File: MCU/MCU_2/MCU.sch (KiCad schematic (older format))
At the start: 41 parts, among them J10 RotEnc, J2 Conn_01x08, J3 Conn_02x20_Odd_Even, J4 SWD, U1 74HC04, U2 STM32F407VETx, Y1 12MHz

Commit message: MCU PCB start layouting
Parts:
- J2: value Conn_01x08 -> LPF
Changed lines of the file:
@@
 P 1800 5350
 F 0 "J2" V 1764 5730 50  0000 L CNN
-F 1 "Conn_01x08" V 1673 5730 50  0000 L CNN
+F 1 "LPF" V 1673 5730 50  0000 L CNN
 F 2 "Connector_JST:JST_PH_B8B-PH-SM4-TB_1x08-1MP_P2.00mm_Vertical" H 1800 5350 50  0001 C CNN
 F 3 "~" H 1800 5350 50  0001 C CNN
@@
 	6050 7250 6050 7400
 $Comp
-L power:GND #PWR?
+L power:GND #PWR0121
 U 1 1 62014679
 P 6150 7300
-F 0 "#PWR?" H 6150 7050 50  0001 C CNN
+F 0 "#PWR0121" H 6150 7050 50  0001 C CNN
 F 1 "GND" V 6155 7172 50  0000 R CNN
 F 2 "" H 6150 7300 50  0001 C CNN
@@
 	6150 7350 6150 7400
 $Comp
-L power:GND #PWR?
+L power:GND #PWR0131
 U 1 1 62098915
 P 5700 7400
-F 0 "#PWR?" H 5700 7150 50  0001 C CNN
+F 0 "#PWR0131" H 5700 7150 50  0001 C CNN
 F 1 "GND" V 5705 7272 50  0000 R CNN
 F 2 "" H 5700 7400 50  0001 C CNN

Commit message: routing signals
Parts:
- removed C5: 104, lc_lib:0805_C, symbol Device:C_Small
- removed L2, L3, L6, L7: 600Ohm, lc_lib:0805_L, symbol Device:Ferrite_Bead_Small
- added C37, C40: 104, lc_lib:0805_C, symbol Device:C_Small
- C1, C2: value C_Small -> 20
- J4: footprint Connector_JST:JST_PH_B4B-PH-SM4-TB_1x04-1MP_P2.00mm_Vertical -> Connector_PinHeader_2.54mm:PinHeader_1x04_P2.54mm_Vertical
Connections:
- net +3V3: now also C37.2, C40.1
- net GNDD: now also C37.1, C40.2
- net RX: now also U2.69 (PA10)
- net RX3: now also U2.48 (PB11)
- net TX: now also U2.68 (PA9)
- net TX3: now also U2.47 (PB10)
- net \PTT_SUPPRESS: now also U2.87 (PD6); no longer U2.65 (PC8)
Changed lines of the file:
@@
 P 3200 3100
 F 0 "C2" V 2971 3100 50  0000 C CNN
-F 1 "C_Small" V 3062 3100 50  0000 C CNN
+F 1 "20" V 3062 3100 50  0000 C CNN
 F 2 "lc_lib:0805_C" H 3200 3100 50  0001 C CNN
 F 3 "~" H 3200 3100 50  0001 C CNN
@@
 P 3200 2900
 F 0 "C1" V 2971 2900 50  0000 C CNN
-F 1 "C_Small" V 3062 2900 50  0000 C CNN
+F 1 "20" V 3062 2900 50  0000 C CNN
 F 2 "lc_lib:0805_C" H 3200 2900 50  0001 C CNN
 F 3 "~" H 3200 2900 50  0001 C CNN
@@
 $EndSheet
 $Sheet
-S 7950 2550 2150 1400
-U 5E7D94C5
-F0 "OutputSignals" 50
-F1 "OutputSignals.sch" 50
-F2 "ALC_trig" I L 7950 2800 50
-F3 "Transmit" O L 7950 3000 50
-F4 "\\PTT" I L 7950 3750 50
-F5 "\\Fatal" I L 7950 3200 50
-$EndSheet
-$Sheet
 S 7950 4650 2150 850
 U 5EA95119
 F0 "ExternalInput" 50
 F1 "ExternalInput.sch" 50
-F2 "BAND" O L 7950 4900 50
-F3 "TX" O L 7950 5250 50
-F4 "RX" O L 7950 5350 50
-F5 "CAN_TX" I R 10100 5350 50
-F6 "CAN_RX" O R 10100 5200 50
-F7 "TX_R" I R 10100 5000 50
-F8 "RX_R" O R 10100 4850 50
-F9 "\\PTT_SUPPRESS" I L 7950 4750 50
-F10 "\\PTT_OUT" O L 7950 5100 50
-F11 "\\Fatal" I L 7950 5450 50
+F2 "TX" O L 7950 5250 50
+F3 "RX" O L 7950 5350 50
+F4 "CAN_TX" I R 10100 5350 50
+F5 "CAN_RX" O R 10100 5200 50
+F6 "TX_R" I R 10100 5000 50
+F7 "RX_R" O R 10100 4850 50
+F8 "\\PTT_SUPPRESS" I L 7950 4750 50
+F9 "\\PTT_OUT" O L 7950 5100 50
+F10 "\\Fatal" I L 7950 5450 50
 $EndSheet
 Text Label 5800 1850 0    50   ~ 0
@@
 Wire Wire Line
 	5700 4950 5800 4950
-Wire Wire Line
-	6250 4250 6100 4250
 Text Label 5800 1650 0    50   ~ 0
 ADC3_1
@@
 Wire Wire Line
 	5000 1100 5100 1100
-$Comp
-L Device:C_Small C6
-U 1 1 5EBD54F8
-P 3850 900
-F 0 "C6" H 3942 946 50  0000 L CNN
-F 1 "104" H 3942 855 50  0000 L CNN
-F 2 "lc_lib:0805_C" H 3850 900 50  0001 C CNN
-F 3 "~" H 3850 900 50  0001 C CNN
-	1    3850 900
-	1    0    0    -1
-$EndComp
 $Comp
 L Device:C_Small C7
@@
 $EndComp
 $Comp
-L Device:C_Small C5
-U 1 1 5EBD698B
-P 3700 900
-F 0 "C5" H 3792 946 50  0000 L CNN
-F 1 "104" H 3792 855 50  0000 L CNN
-F 2 "lc_lib:0805_C" H 3700 900 50  0001 C CNN
-F 3 "~" H 3700 900 50  0001 C CNN
-	1    3700 900
-	1    0    0    -1
-$EndComp
-$Comp
 L Device:C_Small C4
 U 1 1 5EBD6DBD
@@
 Wire Wire Line
 	4300 800  4150 800
-Wire Wire Line
-	3550 1000 3700 1000
 Connection ~ 4300 1000
-Connection ~ 3700 1000
-Wire Wire Line
-	3700 1000 3850 1000
 Connection ~ 3850 1000
 Wire Wire Line
@@
 Wire Wire Line
 	5800 4750 5700 4750
-Text Label 7800 4900 2    50   ~ 0
-ADC3_1
-Wire Wire Line
-	7800 4900 7950 4900
-Text Label 6600 2400 0    50   ~ 0
+Text Label 6300 2400 0    50   ~ 0
 TX
-Text Label 6600 2550 0    50   ~ 0
+Text Label 6300 2550 0    50   ~ 0
 RX
 Text Label 7800 5250 0    50   ~ 0
@@
 F 0 "J4" H 7230 3392 50  0000 L CNN
 F 1 "SWD" H 7230 3301 50  0000 L CNN
-F 2 "Connector_JST:JST_PH_B4B-PH-SM4-TB_1x04-1MP_P2.00mm_Vertical" H 7150 3400 50  0001 C CNN
+F 2 "Connector_PinHeader_2.54mm:PinHeader_1x04_P2.54mm_Vertical" H 7150 3400 50  0001 C CNN
 F 3 "~" H 7150 3400 50  0001 C CNN
 	1    7150 3400
@@
 Wire Wire Line
 	6300 4150 5700 4150
-$Comp
-L Device:Ferrite_Bead_Small L2
-U 1 1 5E2775FC
-P 6400 2400
-F 0 "L2" V 6163 2400 50  0000 C CNN
-F 1 "600Ohm" V 6254 2400 50  0000 C CNN
-F 2 "lc_lib:0805_L" V 6330 2400 50  0001 C CNN
-F 3 "~" H 6400 2400 50  0001 C CNN
-	1    6400 2400
-	0    1    1    0
-$EndComp
-$Comp
-L Device:Ferrite_Bead_Small L3
-U 1 1 5E277E4F
-P 6400 2550
-F 0 "L3" V 6500 2500 50  0000 C CNN
-F 1 "600Ohm" V 6500 2750 50  0000 C CNN
-F 2 "lc_lib:0805_L" V 6330 2550 50  0001 C CNN
-F 3 "~" H 6400 2550 50  0001 C CNN
-	1    6400 2550
-	0    1    1    0
-$EndComp
-Wire Wire Line
-	6600 2550 6500 2550
-Wire Wire Line
-	6600 2400 6500 2400
 Wire Wire Line
 	5700 2550 6300 2550
@@
 Wire Wire Line
 	3800 3350 3900 3350
-Text Label 6350 4350 2    50   ~ 0
+Text Label 6000 4350 2    50   ~ 0
 RX3
-Text Label 6250 4250 0    50   ~ 0
+Text Label 5900 4250 0    50   ~ 0
 TX3
 Text Label 6050 1200 1    50   ~ 0
@@
 Wire Wire Line
 	10300 5000 10100 5000
-$Comp
-L Device:Ferrite_Bead_Small L7
-U 1 1 626356E7
-P 6100 4350
-F 0 "L7" V 5950 4200 50  0000 C CNN
-F 1 "600Ohm" V 6050 4100 50  0000 C CNN
-F 2 "lc_lib:0805_L" V 6030 4350 50  0001 C CNN
-F 3 "~" H 6100 4350 50  0001 C CNN
-	1    6100 4350
-	0    -1   -1   0
-$EndComp
-Wire Wire Line
-	6350 4350 6200 4350
 Wire Wire Line
 	6000 4350 5700 4350
-$Comp
-L Device:Ferrite_Bead_Small L6
-U 1 1 6269B499
-P 6000 4250
-F 0 "L6" V 5950 4400 50  0000 C CNN
-F 1 "600Ohm" V 5950 4050 50  0000 C CNN
-F 2 "lc_lib:0805_L" V 5930 4250 50  0001 C CNN
-F 3 "~" H 6000 4250 50  0001 C CNN
-	1    6000 4250
-	0    1    1    0
-$EndComp
 Wire Wire Line
 	5900 4250 5700 4250
@@
 Wire Wire Line
 	5800 5850 5700 5850
-Text GLabel 5850 5750 2    50   Output ~ 0
+Text GLabel 3700 5550 0    50   Output ~ 0
 \PTT_SUPPRESS
-Wire Wire Line
-	5850 5750 5700 5750
 Text GLabel 7850 4750 0    50   Input ~ 0
 \PTT_SUPPRESS
@@
 Wire Wire Line
 	6350 7000 6900 7000
+Wire Wire Line
+	3700 5550 3900 5550
+$Comp
+L Device:C_Small C37
+U 1 1 61F032A5
+P 3400 900
+F 0 "C37" H 3492 946 50  0000 L CNN
+F 1 "104" H 3492 855 50  0000 L CNN
+F 2 "lc_lib:0805_C" H 3400 900 50  0001 C CNN
+F 3 "~" H 3400 900 50  0001 C CNN
+	1    3400 900
+	1    0    0    1
+$EndComp
+Wire Wire Line
+	3400 800  3550 800
+Connection ~ 3550 800
+Wire Wire Line
+	3400 1000 3550 1000
+Connection ~ 3550 1000
+$Comp
+L Device:C_Small C40
+U 1 1 61F6254A
+P 3500 700
+F 0 "C40" H 3592 746 50  0000 L CNN
+F 1 "104" H 3592 655 50  0000 L CNN
+F 2 "lc_lib:0805_C" H 3500 700 50  0001 C CNN
+F 3 "~" H 3500 700 50  0001 C CNN
+	1    3500 700
+	0    1    -1   0
+$EndComp
+Wire Wire Line
+	3600 700  3700 700
+Connection ~ 3700 700
+Wire Wire Line
+	3400 700  3300 700
+Wire Wire Line
+	3300 700  3300 1000
+Wire Wire Line
+	3300 1000 3400 1000
+Connection ~ 3400 1000
+$Comp
+L Device:C_Small C6
+U 1 1 5EBD54F8
+P 3850 900
+F 0 "C6" H 3942 946 50  0000 L CNN
+F 1 "104" H 3942 855 50  0000 L CNN
+F 2 "lc_lib:0805_C" H 3850 900 50  0001 C CNN
+F 3 "~" H 3850 900 50  0001 C CNN
+	1    3850 900
+	1    0    0    -1
+$EndComp
+Wire Wire Line
+	3550 1000 3850 1000
+$Sheet
+S 7950 2550 2150 1400
+U 5E7D94C5
+F0 "OutputSignals" 50
+F1 "OutputSignals.sch" 50
+F2 "ALC_trig" I L 7950 2800 50
+F3 "Transmit" O L 7950 3000 50
+F4 "\\PTT" I L 7950 3750 50
+F5 "\\Fatal" I L 7950 3200 50
+$EndSheet
 $EndSCHEMATC

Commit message: almost finished routing MCU2
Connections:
- net AUTO_BAND renamed RF_bias_on
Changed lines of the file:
@@
 F23 "PWR_On" I R 10100 900 50
 F24 "\\Fatal" O R 10100 750 50
+F25 "RF_bias_on" I L 8050 2050 50
 $EndSheet
 $Sheet
@@
 Wire Wire Line
 	1800 7000 3250 7000
-Text GLabel 5800 6350 2    50   Input ~ 0
-AUTO_BAND
-Wire Wire Line
-	5800 6350 5700 6350
+Wire Wire Line
+	6100 6350 5700 6350
 Text GLabel 5800 6250 2    50   Output ~ 0
 SEL1
@@
 F5 "\\Fatal" I L 7950 3200 50
 $EndSheet
+Text Label 7550 2050 0    50   ~ 0
+RF_bias_on
+Wire Wire Line
+	7550 2050 8050 2050
+Text Label 7050 2300 0    50   ~ 0
+RF_bias_on
+Text Label 6100 6350 0    50   ~ 0
+RF_bias_on
 $EndSCHEMATC

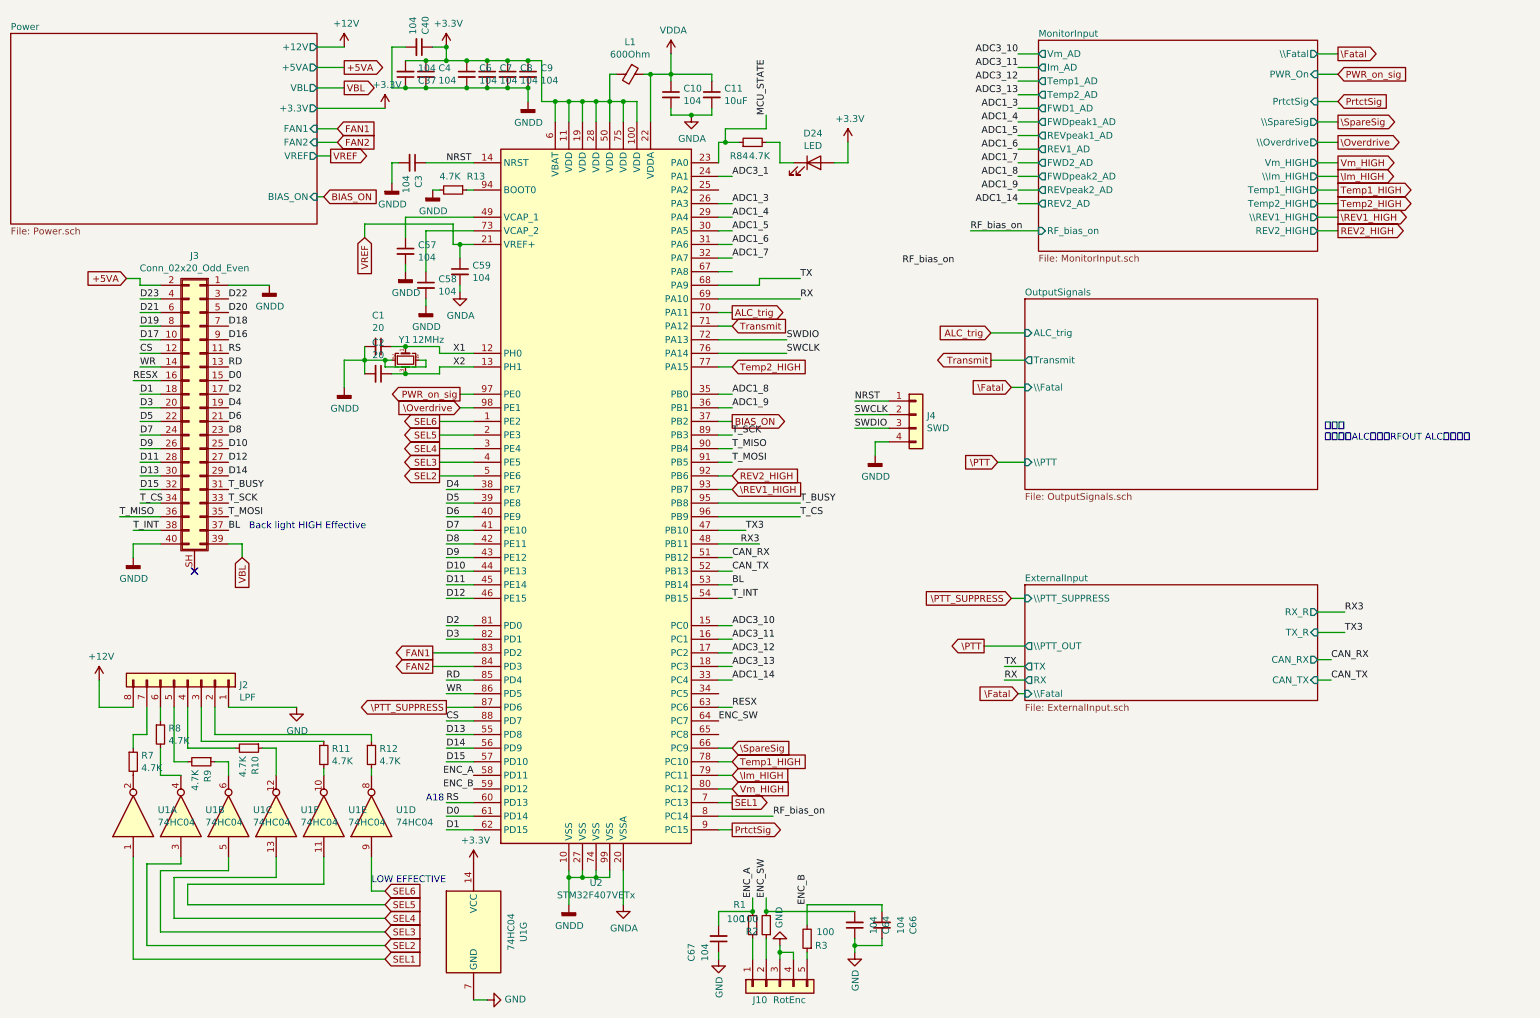
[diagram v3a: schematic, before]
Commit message: added EEPROM to MCU
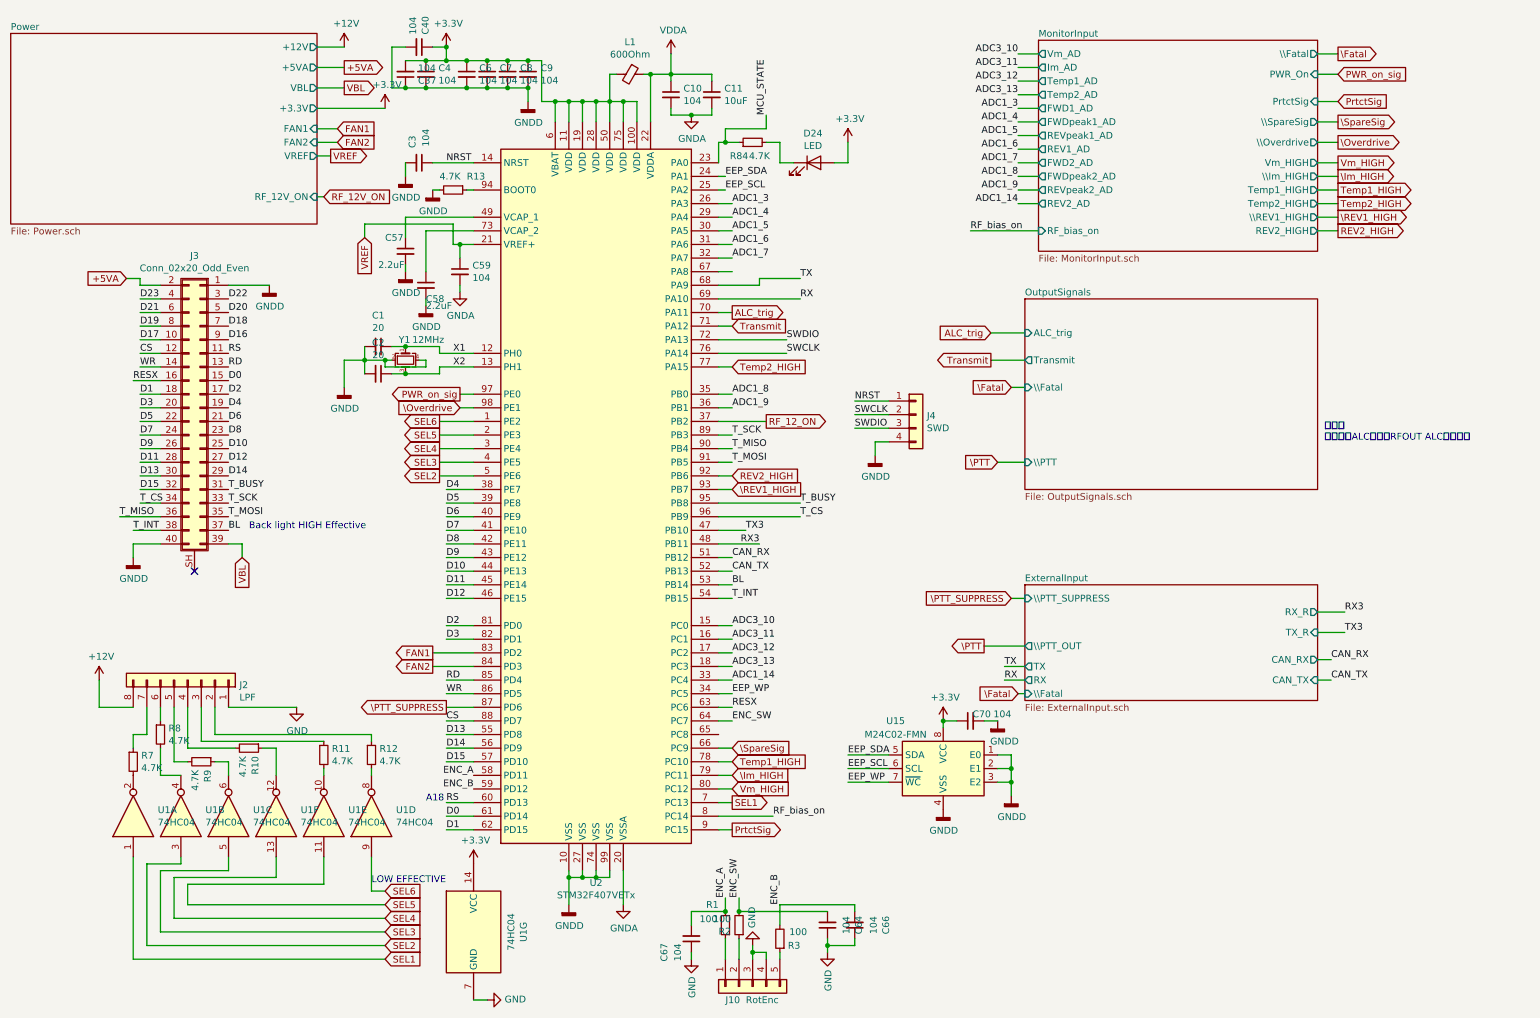
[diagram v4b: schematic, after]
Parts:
- added C70: 104, lc_lib:0805_C, symbol Device:C_Small
- added U15: M24C02-FMN, Package_SO:SOIC-8_3.9x4.9mm_P1.27mm, symbol Memory_EEPROM:M24C02-FMN
- C57, C58: value 104 -> 2.2uF
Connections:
- net +3V3: now also C70.1, U15.8 (VCC)
- net GNDD: now also C70.2, U15.1 (E0), U15.2 (E1), U15.3 (E2), U15.4 (VSS)
- net EEP_SCL: now reaches U2.25 (PA2)
- net EEP_SCL: now also U15.6 (SCL)
- net EEP_WP: now reaches U2.34 (PC5)
- net EEP_WP: now also U15.7 (~WC)
- net ADC3_1 renamed EEP_SDA
- net EEP_SDA: now also U15.5 (SDA)
- net BIAS_ON renamed RF_12_ON
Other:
- moved on the sheet: C3, C64, C66, C67, J10, R1, R2, R3
